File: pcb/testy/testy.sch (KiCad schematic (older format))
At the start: 66 parts, among them SW0:0 SW_Push, SW0:1 SW_Push, SW0:2 SW_Push, SW0:3 SW_Push, SW0:4 SW_Push, SW0:5 SW_Push, SW1:0 SW_Push, SW1:1 SW_Push, SW1:2 SW_Push, SW1:3 SW_Push, SW1:4 SW_Push, SW1:5 SW_Push, SW2:0 SW_Push, SW2:1 SW_Push, SW2:2 SW_Push, SW2:3 SW_Push, SW2:4 SW_Push, SW2:5 SW_Push, SW3:0 SW_Push, SW3:1 SW_Push, SW3:2 SW_Push, SW3:3 SW_Push, SW3:4 SW_Push, SW3:5 SW_Push, SW3:6 SW_Push, SW4:1 SW_Push, SW4:2 SW_Push, SW4:3 SW_Push, SW4:4 SW_Push, U1 ProMicro

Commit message: fix: get TRRS schematic to line up with footprint
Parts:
- TRRS1: renamed from J?; footprint (none) -> footprints:TRRS-PJ-320A-dual
- renumbered D3:6 to D4:6, SW-reset to SW-reset1, SW3:6 to SW4:6
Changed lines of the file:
@@
 Row3
 $Comp
-L mj-4pp-9:MJ-4PP-9 J?
+L mj-4pp-9:MJ-4PP-9 TRRS1
 U 1 1 5DB680F2
 P 2100 6400
-F 0 "J?" H 1622 6327 60  0000 R CNN
+F 0 "TRRS1" H 1622 6327 60  0000 R CNN
 F 1 "MJ-4PP-9" H 1622 6433 60  0000 R CNN
-F 2 "" H 2100 6400 60  0000 C CNN
+F 2 "footprints:TRRS-PJ-320A-dual" H 2100 6400 60  0000 C CNN
 F 3 "" H 2100 6400 60  0000 C CNN
 	1    2100 6400
@@
 data
 $Comp
-L power:GND #PWR?
+L power:GND #PWR0101
 U 1 1 5DB6F1F7
 P 700 2350
-F 0 "#PWR?" H 700 2100 50  0001 C CNN
+F 0 "#PWR0101" H 700 2100 50  0001 C CNN
 F 1 "GND" H 705 2177 50  0000 C CNN
 F 2 "" H 700 2350 50  0001 C CNN
@@
 Row4
 $Comp
-L power:VCC #PWR?
+L power:VCC #PWR0102
 U 1 1 5DB780CB
 P 2750 1950
-F 0 "#PWR?" H 2750 1800 50  0001 C CNN
+F 0 "#PWR0102" H 2750 1800 50  0001 C CNN
 F 1 "VCC" H 2767 2123 50  0000 C CNN
 F 2 "" H 2750 1950 50  0001 C CNN
@@
 Wire Wire Line
 	2750 2200 2750 1950
-Text GLabel 1650 6200 0    50   Input ~ 0
+Text GLabel 1350 6200 0    50   Input ~ 0
 data
 $Comp
-L power:VCC #PWR?
+L power:VCC #PWR0103
 U 1 1 5DB7BCAC
 P 1150 6550
-F 0 "#PWR?" H 1150 6400 50  0001 C CNN
+F 0 "#PWR0103" H 1150 6400 50  0001 C CNN
 F 1 "VCC" H 1168 6723 50  0000 C CNN
 F 2 "" H 1150 6550 50  0001 C CNN
@@
 $EndComp
 $Comp
-L power:GND #PWR?
+L power:GND #PWR0104
 U 1 1 5DB7C36F
 P 1000 6300
-F 0 "#PWR?" H 1000 6050 50  0001 C CNN
+F 0 "#PWR0104" H 1000 6050 50  0001 C CNN
 F 1 "GND" H 1005 6127 50  0000 C CNN
 F 2 "" H 1000 6300 50  0001 C CNN
@@
 	1150 6400 1150 6550
 $Comp
-L Switch:SW_Push SW-reset
+L Switch:SW_Push SW-reset1
 U 1 1 5DB80D38
 P 1650 4000
-F 0 "SW-reset" H 1650 4285 50  0000 C CNN
+F 0 "SW-reset1" H 1650 4285 50  0000 C CNN
 F 1 "SW_Push" H 1650 4194 50  0000 C CNN
 F 2 "footprints:TACT_SWITCH_TVBP06" H 1650 4200 50  0001 C CNN
@@
 Reset
 $Comp
-L power:GND #PWR?
+L power:GND #PWR0105
 U 1 1 5DB88784
 P 1450 4000
-F 0 "#PWR?" H 1450 3750 50  0001 C CNN
+F 0 "#PWR0105" H 1450 3750 50  0001 C CNN
 F 1 "GND" H 1455 3827 50  0000 C CNN
 F 2 "" H 1450 4000 50  0001 C CNN
@@
 Connection ~ 8450 4650
 $Comp
-L Switch:SW_Push SW3:6
+L Switch:SW_Push SW4:6
 U 1 1 5DBF1719
 P 10050 4350
-F 0 "SW3:6" H 10050 4635 50  0000 C CNN
+F 0 "SW4:6" H 10050 4635 50  0000 C CNN
 F 1 "SW_Push" H 10050 4544 50  0000 C CNN
 F 2 "footprints:Kailh_socket_reversible" H 10050 4550 50  0001 C CNN
@@
 	9850 3650 9850 4350
 $Comp
-L Diode:1N4148 D3:6
+L Diode:1N4148 D4:6
 U 1 1 5DBF1724
 P 10250 4500
-F 0 "D3:6" V 10296 4421 50  0000 R CNN
+F 0 "D4:6" V 10296 4421 50  0000 R CNN
 F 1 "1N4148" V 10205 4421 50  0000 R CNN
 F 2 "Diode_THT:D_DO-35_SOD27_P7.62mm_Horizontal" H 10250 4325 50  0001 C CNN
@@
 $EndComp
 $Comp
-L power:GND #PWR?
+L power:GND #PWR0106
 U 1 1 5DC68F20
 P 1200 5800
-F 0 "#PWR?" H 1200 5550 50  0001 C CNN
+F 0 "#PWR0106" H 1200 5550 50  0001 C CNN
 F 1 "GND" H 1205 5627 50  0000 C CNN
 F 2 "" H 1200 5800 50  0001 C CNN
@@
 Text GLabel 2250 5650 2    50   Input ~ 0
 LED2
+Wire Wire Line
+	1350 6200 1650 6200
 $EndSCHEMATC

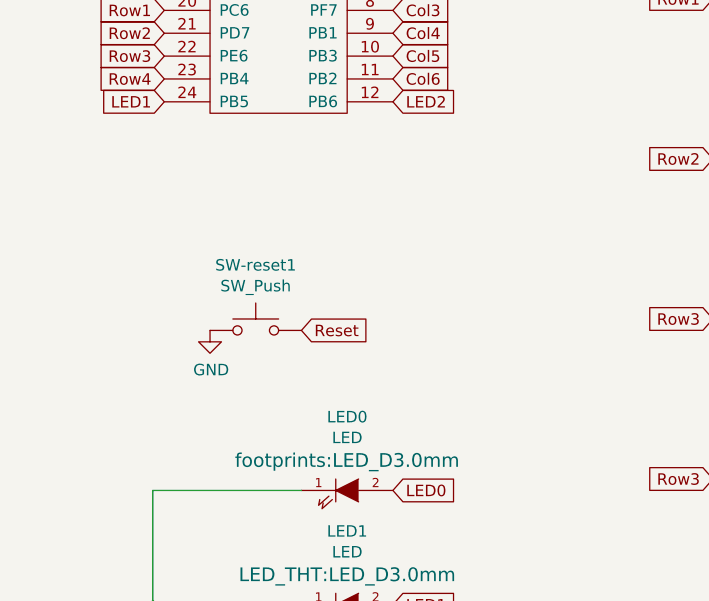
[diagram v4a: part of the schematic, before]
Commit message: chore: add some 4 pin reset switches, played with new footprints
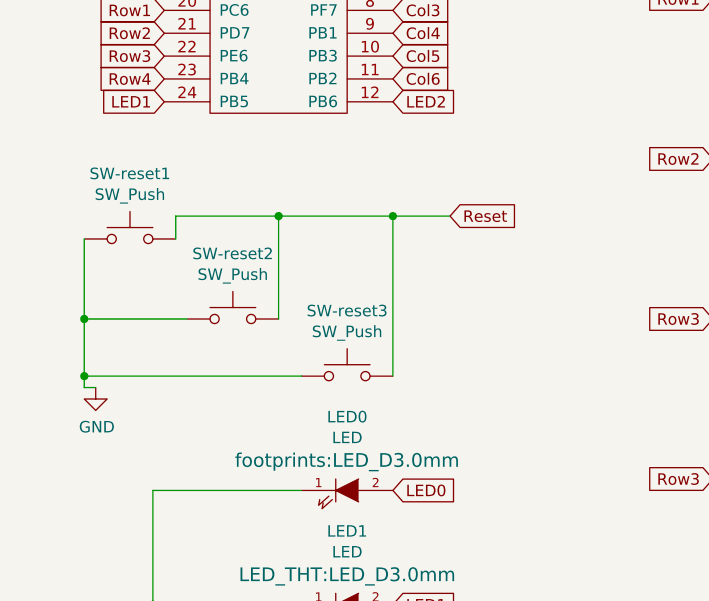
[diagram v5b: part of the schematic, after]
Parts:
- added SW-reset1, SW-reset3: SW_Push, footprints:TACT_SWITCH_TVBP06, symbol Switch:SW_Push
- U1: footprint footprints:ProMicro -> footprints:Pro_Micro_ergotravel
- renumbered SW-reset1 to SW-reset2
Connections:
- net GND: now also SW-reset1.1, SW-reset3.1
- net Reset: now also SW-reset1.2, SW-reset3.2
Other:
- moved on the sheet: SW-reset2
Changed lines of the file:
@@
 F 0 "U1" H 1750 2847 60  0000 C CNN
 F 1 "ProMicro" H 1750 2741 60  0000 C CNN
-F 2 "footprints:ProMicro" H 1750 2250 60  0001 C CNN
+F 2 "footprints:Pro_Micro_ergotravel" H 1750 2250 60  0001 C CNN
 F 3 "" H 1750 2250 60  0001 C CNN
 	1    1750 2250
@@
 	1150 6400 1150 6550
 $Comp
-L Switch:SW_Push SW-reset1
+L Switch:SW_Push SW-reset2
 U 1 1 5DB80D38
-P 1650 4000
-F 0 "SW-reset1" H 1650 4285 50  0000 C CNN
-F 1 "SW_Push" H 1650 4194 50  0000 C CNN
-F 2 "footprints:TACT_SWITCH_TVBP06" H 1650 4200 50  0001 C CNN
-F 3 "~" H 1650 4200 50  0001 C CNN
-	1    1650 4000
+P 1550 3950
+F 0 "SW-reset2" H 1550 4235 50  0000 C CNN
+F 1 "SW_Push" H 1550 4144 50  0000 C CNN
+F 2 "footprints:TACT_SWITCH_TVBP06" H 1550 4150 50  0001 C CNN
+F 3 "~" H 1550 4150 50  0001 C CNN
+	1    1550 3950
 	1    0    0    -1
 $EndComp
 Text GLabel 2250 2100 2    50   Input ~ 0
 Reset
-Text GLabel 1850 4000 2    50   Input ~ 0
+Text GLabel 2500 3500 2    50   Input ~ 0
 Reset
 $Comp
 L power:GND #PWR0105
 U 1 1 5DB88784
-P 1450 4000
-F 0 "#PWR0105" H 1450 3750 50  0001 C CNN
-F 1 "GND" H 1455 3827 50  0000 C CNN
-F 2 "" H 1450 4000 50  0001 C CNN
-F 3 "" H 1450 4000 50  0001 C CNN
-	1    1450 4000
+P 950 4250
+F 0 "#PWR0105" H 950 4000 50  0001 C CNN
+F 1 "GND" H 955 4077 50  0000 C CNN
+F 2 "" H 950 4250 50  0001 C CNN
+F 3 "" H 950 4250 50  0001 C CNN
+	1    950  4250
 	1    0    0    -1
 $EndComp
@@
 Wire Wire Line
 	1350 6200 1650 6200
+$Comp
+L Switch:SW_Push SW-reset1
+U 1 1 5DBAFB80
+P 1100 3600
+F 0 "SW-reset1" H 1100 3885 50  0000 C CNN
+F 1 "SW_Push" H 1100 3794 50  0000 C CNN
+F 2 "footprints:TACT_SWITCH_TVBP06" H 1100 3800 50  0001 C CNN
+F 3 "~" H 1100 3800 50  0001 C CNN
+	1    1100 3600
+	1    0    0    -1
+$EndComp
+$Comp
+L Switch:SW_Push SW-reset3
+U 1 1 5DBB0450
+P 2050 4200
+F 0 "SW-reset3" H 2050 4485 50  0000 C CNN
+F 1 "SW_Push" H 2050 4394 50  0000 C CNN
+F 2 "footprints:TACT_SWITCH_TVBP06" H 2050 4400 50  0001 C CNN
+F 3 "~" H 2050 4400 50  0001 C CNN
+	1    2050 4200
+	1    0    0    -1
+$EndComp
+Wire Wire Line
+	2500 3500 2250 3500
+Wire Wire Line
+	1300 3500 1300 3600
+Wire Wire Line
+	1750 3950 1750 3500
+Connection ~ 1750 3500
+Wire Wire Line
+	1750 3500 1300 3500
+Wire Wire Line
+	2250 4200 2250 3500
+Connection ~ 2250 3500
+Wire Wire Line
+	2250 3500 1750 3500
+Wire Wire Line
+	900  3600 900  3950
+Wire Wire Line
+	900  4250 950  4250
+Wire Wire Line
+	1350 3950 900  3950
+Connection ~ 900  3950
+Wire Wire Line
+	900  3950 900  4200
+Wire Wire Line
+	1850 4200 900  4200
+Connection ~ 900  4200
+Wire Wire Line
+	900  4200 900  4250
 $EndSCHEMATC

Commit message: feat: remove footprint with solder on for fullsize MX switches, that wasn't ever going to work; fix existing combo footprint to add clearance for choc switches, start the col stagger layout
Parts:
- SW-reset2, SW-reset3: footprint footprints:TACT_SWITCH_TVBP06 -> footprints:SW_TACT_ALPS_SKQGABE010
- SW0:0, SW0:1, SW0:2, SW0:3, SW0:4, SW0:5, SW1:0, SW1:1, SW1:2, SW1:3, SW1:4, SW1:5, SW2:0, SW2:1, SW2:2, SW2:3, SW2:4, SW2:5, SW3:0, SW3:1, SW3:2, SW3:3, SW3:4, SW3:5, SW3:6, SW4:1, SW4:2, SW4:3, SW4:4, SW4:6: footprint footprints:Kailh_socket_reversible -> footprints:kailh-socket-and-choc-solder-reversible
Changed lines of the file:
@@
 F 0 "SW0:0" H 4450 1835 50  0000 C CNN
 F 1 "SW_Push" H 4450 1744 50  0000 C CNN
-F 2 "footprints:Kailh_socket_reversible" H 4450 1750 50  0001 C CNN
+F 2 "footprints:kailh-socket-and-choc-solder-reversible" H 4450 1750 50  0001 C CNN
 F 3 "~" H 4450 1750 50  0001 C CNN
 	1    4450 1550
@@
 F 0 "SW0:1" H 5450 1835 50  0000 C CNN
 F 1 "SW_Push" H 5450 1744 50  0000 C CNN
-F 2 "footprints:Kailh_socket_reversible" H 5450 1750 50  0001 C CNN
+F 2 "footprints:kailh-socket-and-choc-solder-reversible" H 5450 1750 50  0001 C CNN
 F 3 "~" H 5450 1750 50  0001 C CNN
 	1    5450 1550
@@
 F 0 "SW0:2" H 6350 1835 50  0000 C CNN
 F 1 "SW_Push" H 6350 1744 50  0000 C CNN
-F 2 "footprints:Kailh_socket_reversible" H 6350 1750 50  0001 C CNN
+F 2 "footprints:kailh-socket-and-choc-solder-reversible" H 6350 1750 50  0001 C CNN
 F 3 "~" H 6350 1750 50  0001 C CNN
 	1    6350 1550
@@
 F 0 "SW1:1" H 5450 2535 50  0000 C CNN
 F 1 "SW_Push" H 5450 2444 50  0000 C CNN
-F 2 "footprints:Kailh_socket_reversible" H 5450 2450 50  0001 C CNN
+F 2 "footprints:kailh-socket-and-choc-solder-reversible" H 5450 2450 50  0001 C CNN
 F 3 "~" H 5450 2450 50  0001 C CNN
 	1    5450 2250
@@
 F 0 "SW1:2" H 6350 2535 50  0000 C CNN
 F 1 "SW_Push" H 6350 2444 50  0000 C CNN
-F 2 "footprints:Kailh_socket_reversible" H 6350 2450 50  0001 C CNN
+F 2 "footprints:kailh-socket-and-choc-solder-reversible" H 6350 2450 50  0001 C CNN
 F 3 "~" H 6350 2450 50  0001 C CNN
 	1    6350 2250
@@
 F 0 "SW1:0" H 4450 2535 50  0000 C CNN
 F 1 "SW_Push" H 4450 2444 50  0000 C CNN
-F 2 "footprints:Kailh_socket_reversible" H 4450 2450 50  0001 C CNN
+F 2 "footprints:kailh-socket-and-choc-solder-reversible" H 4450 2450 50  0001 C CNN
 F 3 "~" H 4450 2450 50  0001 C CNN
 	1    4450 2250
@@
 F 0 "SW0:3" H 7250 1835 50  0000 C CNN
 F 1 "SW_Push" H 7250 1744 50  0000 C CNN
-F 2 "footprints:Kailh_socket_reversible" H 7250 1750 50  0001 C CNN
+F 2 "footprints:kailh-socket-and-choc-solder-reversible" H 7250 1750 50  0001 C CNN
 F 3 "~" H 7250 1750 50  0001 C CNN
 	1    7250 1550
@@
 F 0 "SW1:3" H 7250 2535 50  0000 C CNN
 F 1 "SW_Push" H 7250 2444 50  0000 C CNN
-F 2 "footprints:Kailh_socket_reversible" H 7250 2450 50  0001 C CNN
+F 2 "footprints:kailh-socket-and-choc-solder-reversible" H 7250 2450 50  0001 C CNN
 F 3 "~" H 7250 2450 50  0001 C CNN
 	1    7250 2250
@@
 F 0 "SW2:0" H 4450 3235 50  0000 C CNN
 F 1 "SW_Push" H 4450 3144 50  0000 C CNN
-F 2 "footprints:Kailh_socket_reversible" H 4450 3150 50  0001 C CNN
+F 2 "footprints:kailh-socket-and-choc-solder-reversible" H 4450 3150 50  0001 C CNN
 F 3 "~" H 4450 3150 50  0001 C CNN
 	1    4450 2950
@@
 F 0 "SW2:1" H 5450 3235 50  0000 C CNN
 F 1 "SW_Push" H 5450 3144 50  0000 C CNN
-F 2 "footprints:Kailh_socket_reversible" H 5450 3150 50  0001 C CNN
+F 2 "footprints:kailh-socket-and-choc-solder-reversible" H 5450 3150 50  0001 C CNN
 F 3 "~" H 5450 3150 50  0001 C CNN
 	1    5450 2950
@@
 F 0 "SW2:2" H 6350 3235 50  0000 C CNN
 F 1 "SW_Push" H 6350 3144 50  0000 C CNN
-F 2 "footprints:Kailh_socket_reversible" H 6350 3150 50  0001 C CNN
+F 2 "footprints:kailh-socket-and-choc-solder-reversible" H 6350 3150 50  0001 C CNN
 F 3 "~" H 6350 3150 50  0001 C CNN
 	1    6350 2950
@@
 F 0 "SW3:1" H 5450 3935 50  0000 C CNN
 F 1 "SW_Push" H 5450 3844 50  0000 C CNN
-F 2 "footprints:Kailh_socket_reversible" H 5450 3850 50  0001 C CNN
+F 2 "footprints:kailh-socket-and-choc-solder-reversible" H 5450 3850 50  0001 C CNN
 F 3 "~" H 5450 3850 50  0001 C CNN
 	1    5450 3650
@@
 F 0 "SW3:2" H 6350 3935 50  0000 C CNN
 F 1 "SW_Push" H 6350 3844 50  0000 C CNN
-F 2 "footprints:Kailh_socket_reversible" H 6350 3850 50  0001 C CNN
+F 2 "footprints:kailh-socket-and-choc-solder-reversible" H 6350 3850 50  0001 C CNN
 F 3 "~" H 6350 3850 50  0001 C CNN
 	1    6350 3650
@@
 F 0 "SW3:0" H 4450 3935 50  0000 C CNN
 F 1 "SW_Push" H 4450 3844 50  0000 C CNN
-F 2 "footprints:Kailh_socket_reversible" H 4450 3850 50  0001 C CNN
+F 2 "footprints:kailh-socket-and-choc-solder-reversible" H 4450 3850 50  0001 C CNN
 F 3 "~" H 4450 3850 50  0001 C CNN
 	1    4450 3650
@@
 F 0 "SW2:3" H 7250 3235 50  0000 C CNN
 F 1 "SW_Push" H 7250 3144 50  0000 C CNN
-F 2 "footprints:Kailh_socket_reversible" H 7250 3150 50  0001 C CNN
+F 2 "footprints:kailh-socket-and-choc-solder-reversible" H 7250 3150 50  0001 C CNN
 F 3 "~" H 7250 3150 50  0001 C CNN
 	1    7250 2950
@@
 F 0 "SW3:3" H 7250 3935 50  0000 C CNN
 F 1 "SW_Push" H 7250 3844 50  0000 C CNN
-F 2 "footprints:Kailh_socket_reversible" H 7250 3850 50  0001 C CNN
+F 2 "footprints:kailh-socket-and-choc-solder-reversible" H 7250 3850 50  0001 C CNN
 F 3 "~" H 7250 3850 50  0001 C CNN
 	1    7250 3650
@@
 F 0 "SW-reset2" H 1550 4235 50  0000 C CNN
 F 1 "SW_Push" H 1550 4144 50  0000 C CNN
-F 2 "footprints:TACT_SWITCH_TVBP06" H 1550 4150 50  0001 C CNN
+F 2 "footprints:SW_TACT_ALPS_SKQGABE010" H 1550 4150 50  0001 C CNN
 F 3 "~" H 1550 4150 50  0001 C CNN
 	1    1550 3950
@@
 F 0 "SW0:4" H 8250 1835 50  0000 C CNN
 F 1 "SW_Push" H 8250 1744 50  0000 C CNN
-F 2 "footprints:Kailh_socket_reversible" H 8250 1750 50  0001 C CNN
+F 2 "footprints:kailh-socket-and-choc-solder-reversible" H 8250 1750 50  0001 C CNN
 F 3 "~" H 8250 1750 50  0001 C CNN
 	1    8250 1550
@@
 F 0 "SW0:5" H 9150 1835 50  0000 C CNN
 F 1 "SW_Push" H 9150 1744 50  0000 C CNN
-F 2 "footprints:Kailh_socket_reversible" H 9150 1750 50  0001 C CNN
+F 2 "footprints:kailh-socket-and-choc-solder-reversible" H 9150 1750 50  0001 C CNN
 F 3 "~" H 9150 1750 50  0001 C CNN
 	1    9150 1550
@@
 F 0 "SW1:4" H 8250 2535 50  0000 C CNN
 F 1 "SW_Push" H 8250 2444 50  0000 C CNN
-F 2 "footprints:Kailh_socket_reversible" H 8250 2450 50  0001 C CNN
+F 2 "footprints:kailh-socket-and-choc-solder-reversible" H 8250 2450 50  0001 C CNN
 F 3 "~" H 8250 2450 50  0001 C CNN
 	1    8250 2250
@@
 F 0 "SW1:5" H 9150 2535 50  0000 C CNN
 F 1 "SW_Push" H 9150 2444 50  0000 C CNN
-F 2 "footprints:Kailh_socket_reversible" H 9150 2450 50  0001 C CNN
+F 2 "footprints:kailh-socket-and-choc-solder-reversible" H 9150 2450 50  0001 C CNN
 F 3 "~" H 9150 2450 50  0001 C CNN
 	1    9150 2250
@@
 F 0 "SW2:4" H 8250 3235 50  0000 C CNN
 F 1 "SW_Push" H 8250 3144 50  0000 C CNN
-F 2 "footprints:Kailh_socket_reversible" H 8250 3150 50  0001 C CNN
+F 2 "footprints:kailh-socket-and-choc-solder-reversible" H 8250 3150 50  0001 C CNN
 F 3 "~" H 8250 3150 50  0001 C CNN
 	1    8250 2950
@@
 F 0 "SW2:5" H 9150 3235 50  0000 C CNN
 F 1 "SW_Push" H 9150 3144 50  0000 C CNN
-F 2 "footprints:Kailh_socket_reversible" H 9150 3150 50  0001 C CNN
+F 2 "footprints:kailh-socket-and-choc-solder-reversible" H 9150 3150 50  0001 C CNN
 F 3 "~" H 9150 3150 50  0001 C CNN
 	1    9150 2950
@@
 F 0 "SW3:4" H 8250 3935 50  0000 C CNN
 F 1 "SW_Push" H 8250 3844 50  0000 C CNN
-F 2 "footprints:Kailh_socket_reversible" H 8250 3850 50  0001 C CNN
+F 2 "footprints:kailh-socket-and-choc-solder-reversible" H 8250 3850 50  0001 C CNN
 F 3 "~" H 8250 3850 50  0001 C CNN
 	1    8250 3650
@@
 F 0 "SW3:5" H 9150 3935 50  0000 C CNN
 F 1 "SW_Push" H 9150 3844 50  0000 C CNN
-F 2 "footprints:Kailh_socket_reversible" H 9150 3850 50  0001 C CNN
+F 2 "footprints:kailh-socket-and-choc-solder-reversible" H 9150 3850 50  0001 C CNN
 F 3 "~" H 9150 3850 50  0001 C CNN
 	1    9150 3650
@@
 F 0 "SW3:6" H 10050 3935 50  0000 C CNN
 F 1 "SW_Push" H 10050 3844 50  0000 C CNN
-F 2 "footprints:Kailh_socket_reversible" H 10050 3850 50  0001 C CNN
+F 2 "footprints:kailh-socket-and-choc-solder-reversible" H 10050 3850 50  0001 C CNN
 F 3 "~" H 10050 3850 50  0001 C CNN
 	1    10050 3650
@@
 F 0 "SW4:1" H 5450 4635 50  0000 C CNN
 F 1 "SW_Push" H 5450 4544 50  0000 C CNN
-F 2 "footprints:Kailh_socket_reversible" H 5450 4550 50  0001 C CNN
+F 2 "footprints:kailh-socket-and-choc-solder-reversible" H 5450 4550 50  0001 C CNN
 F 3 "~" H 5450 4550 50  0001 C CNN
 	1    5450 4350
@@
 F 0 "SW4:2" H 6350 4635 50  0000 C CNN
 F 1 "SW_Push" H 6350 4544 50  0000 C CNN
-F 2 "footprints:Kailh_socket_reversible" H 6350 4550 50  0001 C CNN
+F 2 "footprints:kailh-socket-and-choc-solder-reversible" H 6350 4550 50  0001 C CNN
 F 3 "~" H 6350 4550 50  0001 C CNN
 	1    6350 4350
@@
 F 0 "SW4:3" H 7250 4635 50  0000 C CNN
 F 1 "SW_Push" H 7250 4544 50  0000 C CNN
-F 2 "footprints:Kailh_socket_reversible" H 7250 4550 50  0001 C CNN
+F 2 "footprints:kailh-socket-and-choc-solder-reversible" H 7250 4550 50  0001 C CNN
 F 3 "~" H 7250 4550 50  0001 C CNN
 	1    7250 4350
@@
 F 0 "SW4:4" H 8250 4635 50  0000 C CNN
 F 1 "SW_Push" H 8250 4544 50  0000 C CNN
-F 2 "footprints:Kailh_socket_reversible" H 8250 4550 50  0001 C CNN
+F 2 "footprints:kailh-socket-and-choc-solder-reversible" H 8250 4550 50  0001 C CNN
 F 3 "~" H 8250 4550 50  0001 C CNN
 	1    8250 4350
@@
 F 0 "SW4:6" H 10050 4635 50  0000 C CNN
 F 1 "SW_Push" H 10050 4544 50  0000 C CNN
-F 2 "footprints:Kailh_socket_reversible" H 10050 4550 50  0001 C CNN
+F 2 "footprints:kailh-socket-and-choc-solder-reversible" H 10050 4550 50  0001 C CNN
 F 3 "~" H 10050 4550 50  0001 C CNN
 	1    10050 4350
@@
 F 0 "SW-reset3" H 2050 4485 50  0000 C CNN
 F 1 "SW_Push" H 2050 4394 50  0000 C CNN
-F 2 "footprints:TACT_SWITCH_TVBP06" H 2050 4400 50  0001 C CNN
+F 2 "footprints:SW_TACT_ALPS_SKQGABE010" H 2050 4400 50  0001 C CNN
 F 3 "~" H 2050 4400 50  0001 C CNN
 	1    2050 4200
